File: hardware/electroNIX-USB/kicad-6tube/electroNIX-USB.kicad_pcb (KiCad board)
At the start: 2 copper layers, 150 x 66 mm, 142 parts, among them J1 USB-C (USB 2.0), Q1 MMBT3904, Q10 MMBTA42, Q11 MMBTA92, Q12 MMBTA42, Q13 MMBTA92, Q14 MMBTA42, Q15 MMBTA92, Q16 MMBTA42, Q17 MMBTA42, Q18 MMBTA42, Q19 MMBTA42, Q2 MMBT3904, Q20 MMBTA42, Q21 MMBTA42, Q22 MMBTA42, Q23 MMBTA42, Q24 MMBTA42, Q25 MMBTA42, Q26 MMBTA42, Q27 MMBTA42, Q3 IRLR3110ZPBF, Q4 MMBTA42, Q5 MMBTA92, Q6 MMBTA42, Q7 MMBTA92, Q8 MMBTA42, Q9 MMBTA92, U1 USBLC6-2SC6, U2 AMS1117-3.3, U3 CH340C, U4 ESP32-WROOM-32E-N4

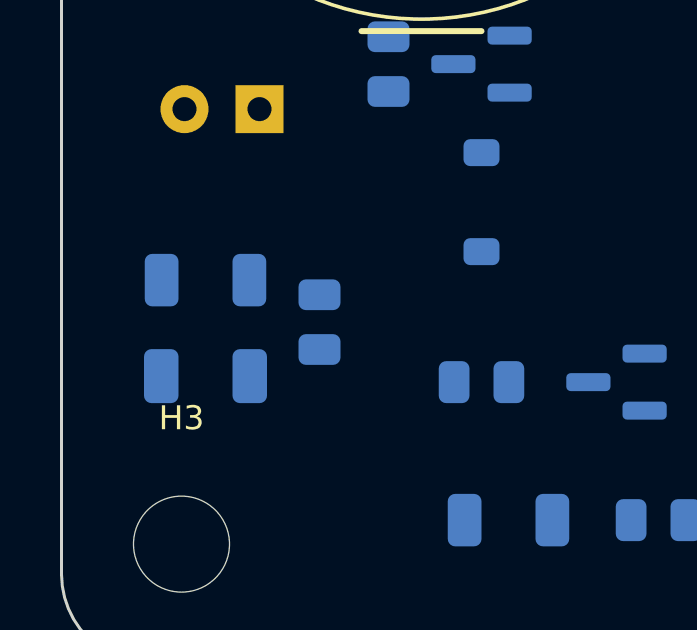
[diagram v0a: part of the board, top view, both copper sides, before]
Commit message: electroNIX-USB: restore PCB-036 KBIAS capacitor string (4 x 470n in series)
C41-C44 on PCB-036 are in series (118 nF, 200 V string) across R46, not
in parallel. Replace the single 2.2 uF/50 V cap with the original series
string and place it beside the 430k/100k divider.

Co-Authored-By: Claude Opus 5.5 <noreply@anthropic.com>
Claude-Session: https://claude.ai/code/session_01AFMfevKEKDGbci8uJGhf4W
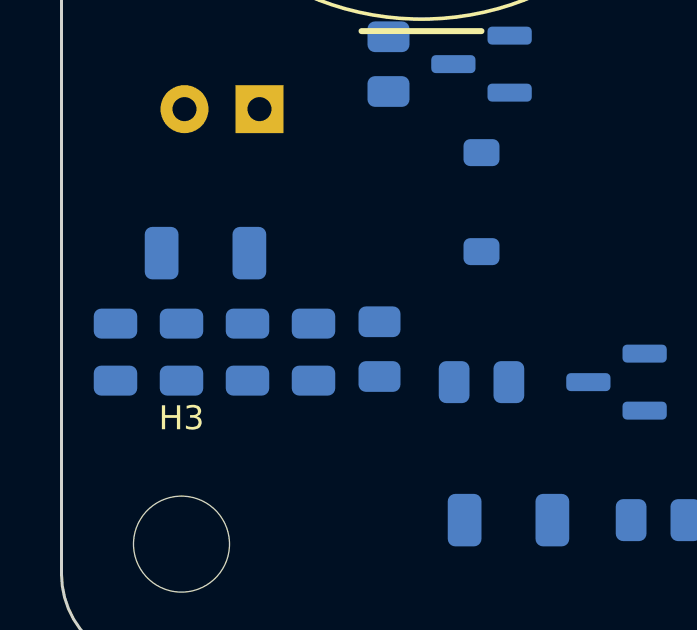
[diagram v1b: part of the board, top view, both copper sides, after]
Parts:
- added C22: 470n 50V, C_0805_2012Metric, B.Cu at (104.0, 155.6)
- added C23: 470n 50V, C_0805_2012Metric, B.Cu at (106.2, 155.6)
- added C24: 470n 50V, C_0805_2012Metric, B.Cu at (108.4, 155.6)
- C21: value 2u2 50V -> 470n 50V; footprint C_1206_3216Metric -> C_0805_2012Metric
- moved C21 3.10 mm to (101.8, 155.6), turned to -90 degrees
- moved R53 2.19 mm to (110.6, 155.5)
- moved R52 0.90 mm to (104.8, 152.3)
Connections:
- C21 pad 2: GND -> Net-(C21-Pad2)

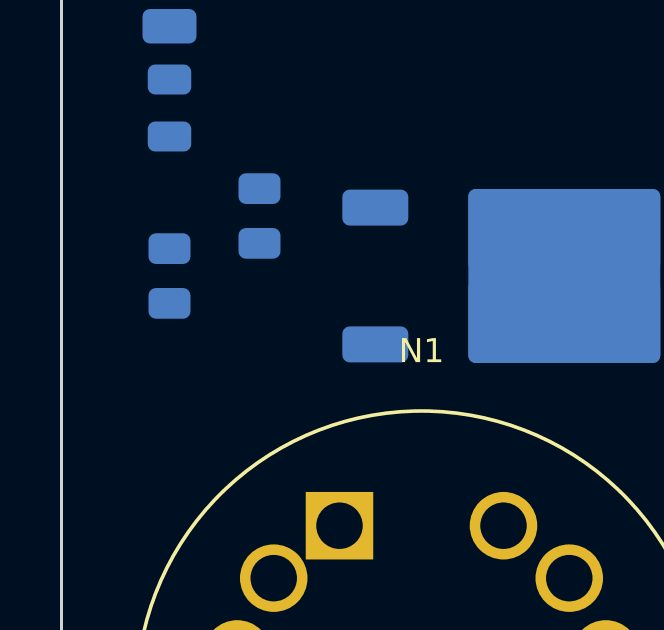
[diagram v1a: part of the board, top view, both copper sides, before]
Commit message: electroNIX-USB: boost gate pull-down gate-to-source as on PCB-036
R45 on PCB-036 pulls the FET gate (after the 10R) to GND; ours sat on
the IO2 side. Move it to the gate and place it at the gate pad. Add a
note listing what was checked against the PCB-036 schematic.

Co-Authored-By: Claude Opus 5.5 <noreply@anthropic.com>
Claude-Session: https://claude.ai/code/session_01AFMfevKEKDGbci8uJGhf4W
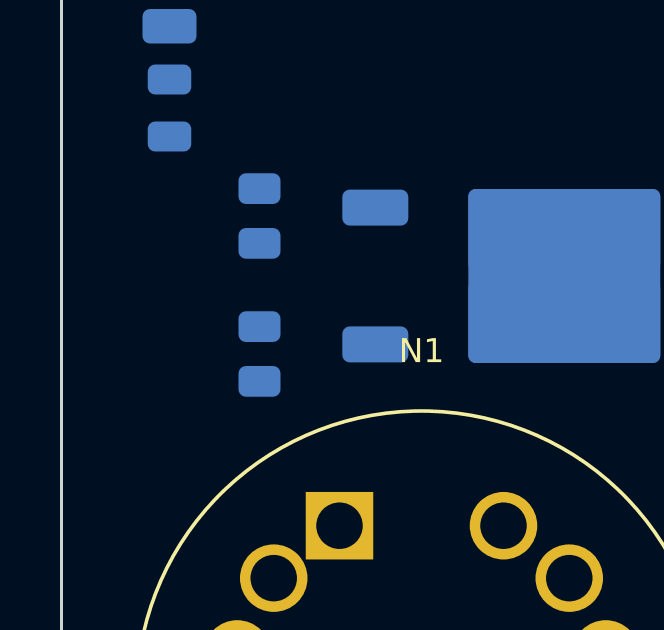
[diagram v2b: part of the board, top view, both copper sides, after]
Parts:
- moved R9 3.97 mm to (106.6, 123.6)
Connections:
- R9 pad 1: PWM -> Net-(Q3-G)

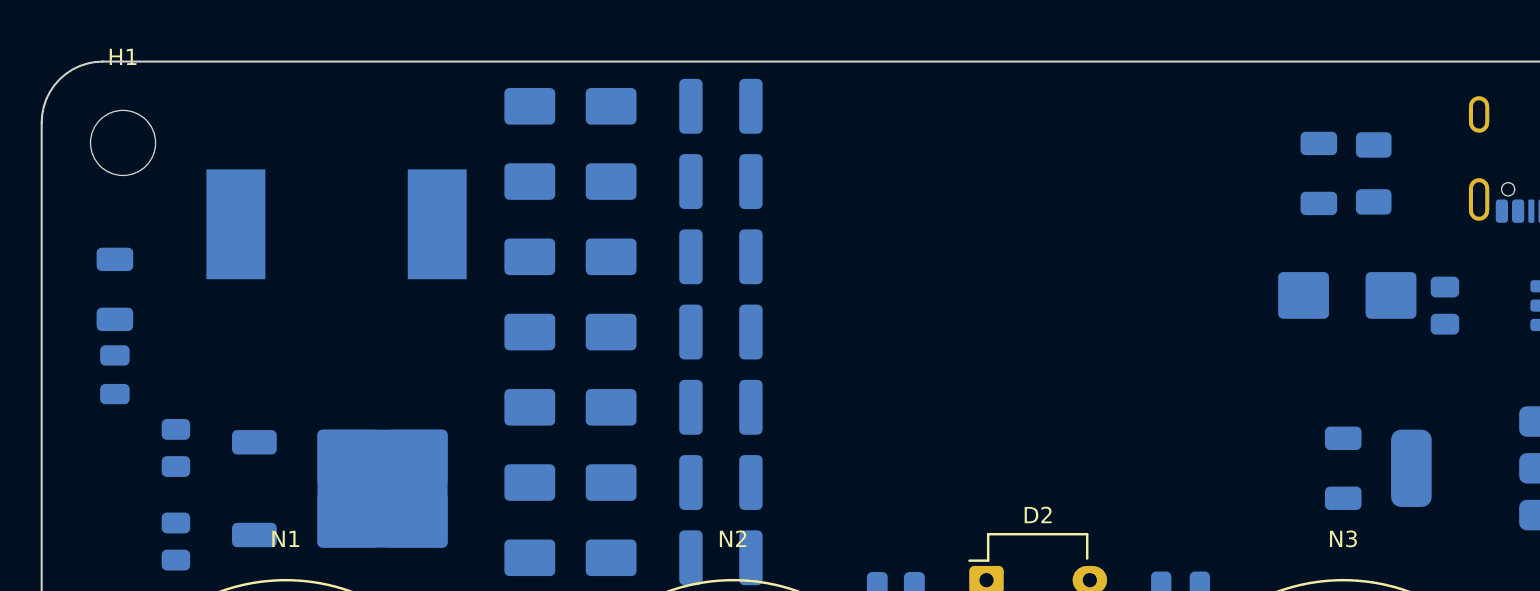
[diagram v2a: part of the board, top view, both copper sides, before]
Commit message: electroNIX-USB: tantalum bulk caps on the 5 V input and boost input
Back to PCB-036's 22 uF/35 V tantalum (7343 D case) for the boost input
and use the same part for the USB-C bulk cap. It holds its value at 5 V,
unlike a small MLCC, and its ESR damps hot-plug ringing on the cable.
The 100 nF ceramics stay. Placement adjusted around the larger parts.

Co-Authored-By: Claude Opus 5.5 <noreply@anthropic.com>
Claude-Session: https://claude.ai/code/session_01AFMfevKEKDGbci8uJGhf4W
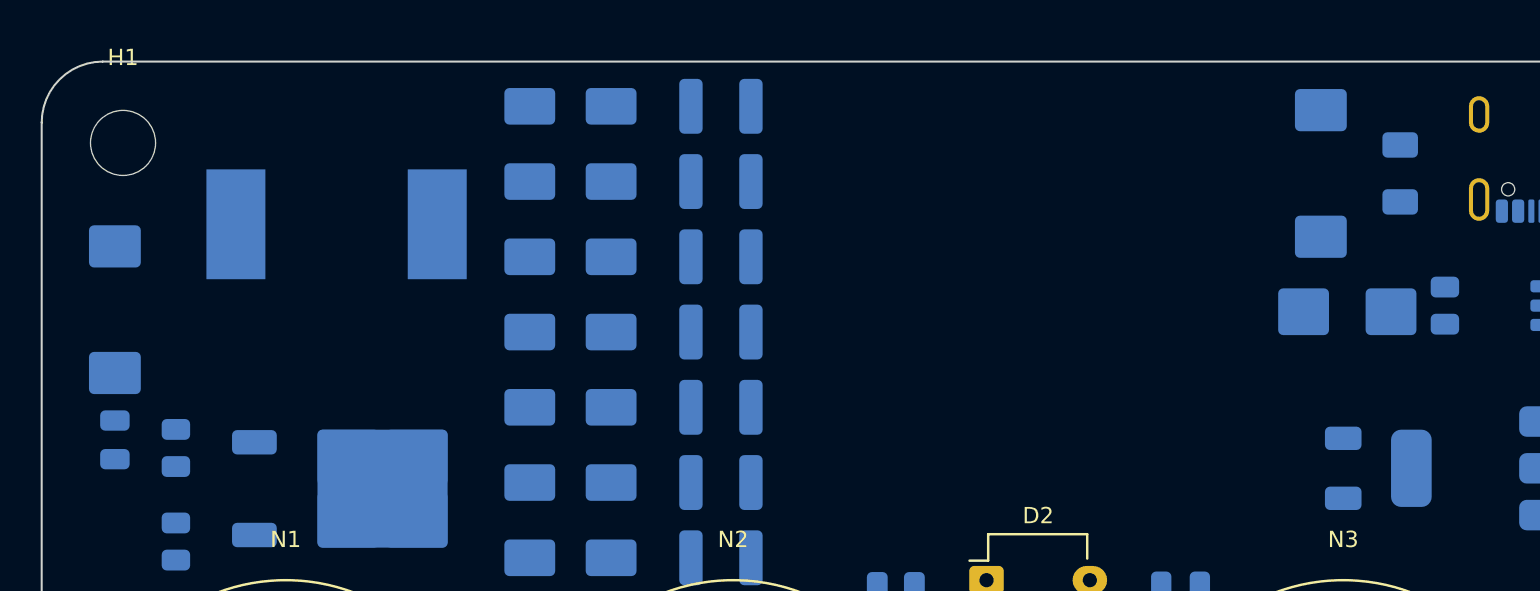
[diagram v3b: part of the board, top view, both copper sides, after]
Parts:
- C1, C10: value 22u 10V -> 22u 35V tant.; footprint C_1206_3216Metric -> CP_EIA-7343-31_Kemet-D
- moved C11 3.20 mm to (103.6, 118.6)
- moved F1 1.30 mm to (166.8, 105.5)
- moved C10 1.00 mm to (103.6, 112.2)
- moved D1 0.80 mm to (164.2, 112.3)
- moved C1 0.10 mm to (162.9, 105.5)

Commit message: electroNIX-USB: lay the 170 V output electrolytic flat
New footprint CP_Radial_D8mm_P2.50mm_Lying (2.5 mm leads, keep-clear for
a body up to 8 x 12.5 mm folded flat). C19 now runs along the left edge
toward the front; KBIAS parts and the cathode row moved right to clear it.

Co-Authored-By: Claude Opus 5.5 <noreply@anthropic.com>
Claude-Session: https://claude.ai/code/session_01AFMfevKEKDGbci8uJGhf4W
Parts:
- C19: footprint CP_Radial_D6.3mm_P2.50mm -> CP_Radial_D8mm_P2.50mm_Lying
- moved C22 11.0 mm to (113.4, 149.8)
- moved C21 10.4 mm to (110.4, 149.8)
- moved R53 10.3 mm to (113.4, 145.6)
- moved R52 8.73 mm to (110.4, 145.6), turned to -90 degrees
- moved C24 5.46 mm to (113.4, 153.4)
- moved D11 5.00 mm to (119.0, 150.6)
- moved Q16 5.00 mm to (119.0, 146.0)
- moved R36 5.00 mm to (115.9, 146.0)
- moved C23 4.74 mm to (110.4, 153.4)
- moved R37 4.45 mm to (129.6, 146.0)
- moved D12 4.44 mm to (132.7, 150.6)
- moved Q17 4.44 mm to (132.7, 146.0)
- moved D13 3.89 mm to (146.3, 150.6)
- moved Q18 3.89 mm to (146.3, 146.0)
- moved R38 3.89 mm to (143.2, 146.0)
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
